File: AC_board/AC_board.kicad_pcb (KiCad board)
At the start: 2 copper layers, 96.5 x 75 mm, 17 parts, among them J1 1226, J2 7471287, J3 Conn_01x02_Male, J4 7471287, J5 7471287, J6 Conn_01x02_Male, K1 G6B-2214P-US-DC12

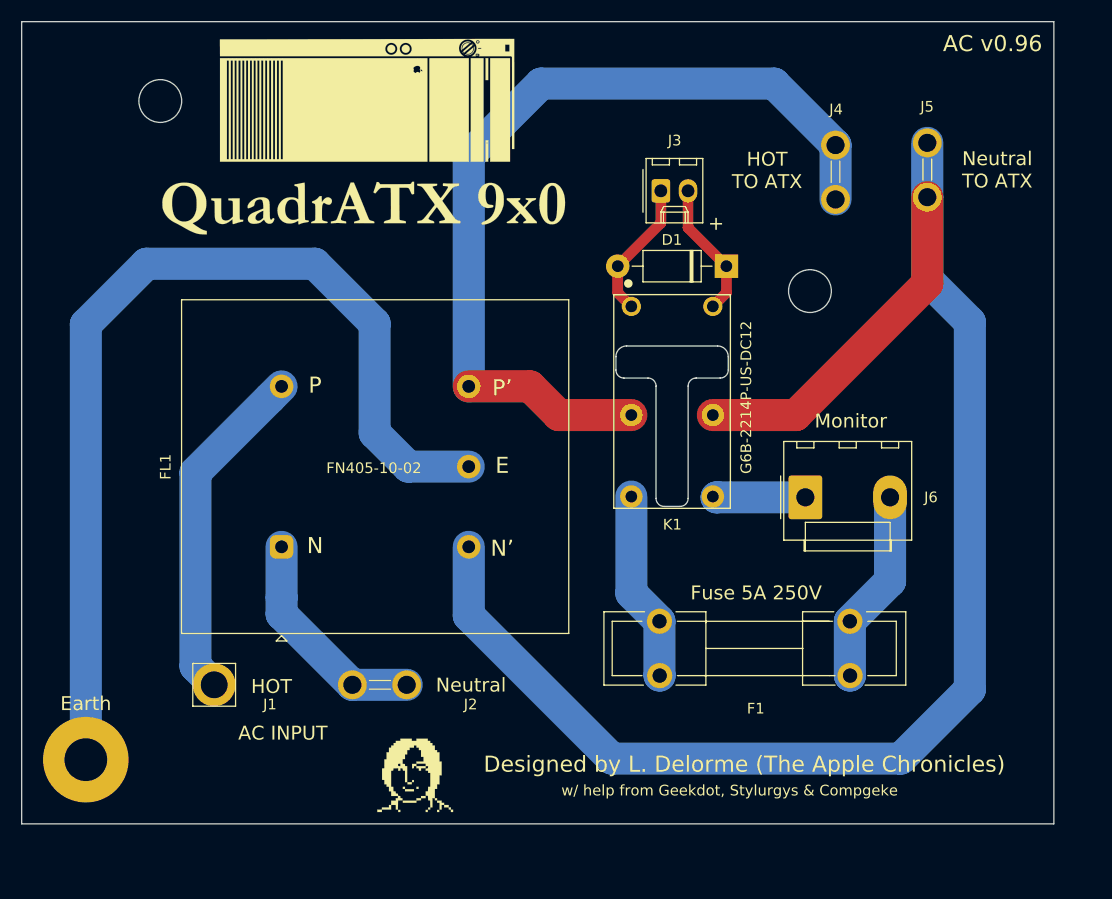
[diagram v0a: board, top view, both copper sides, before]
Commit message: Brand new AC and DC boards
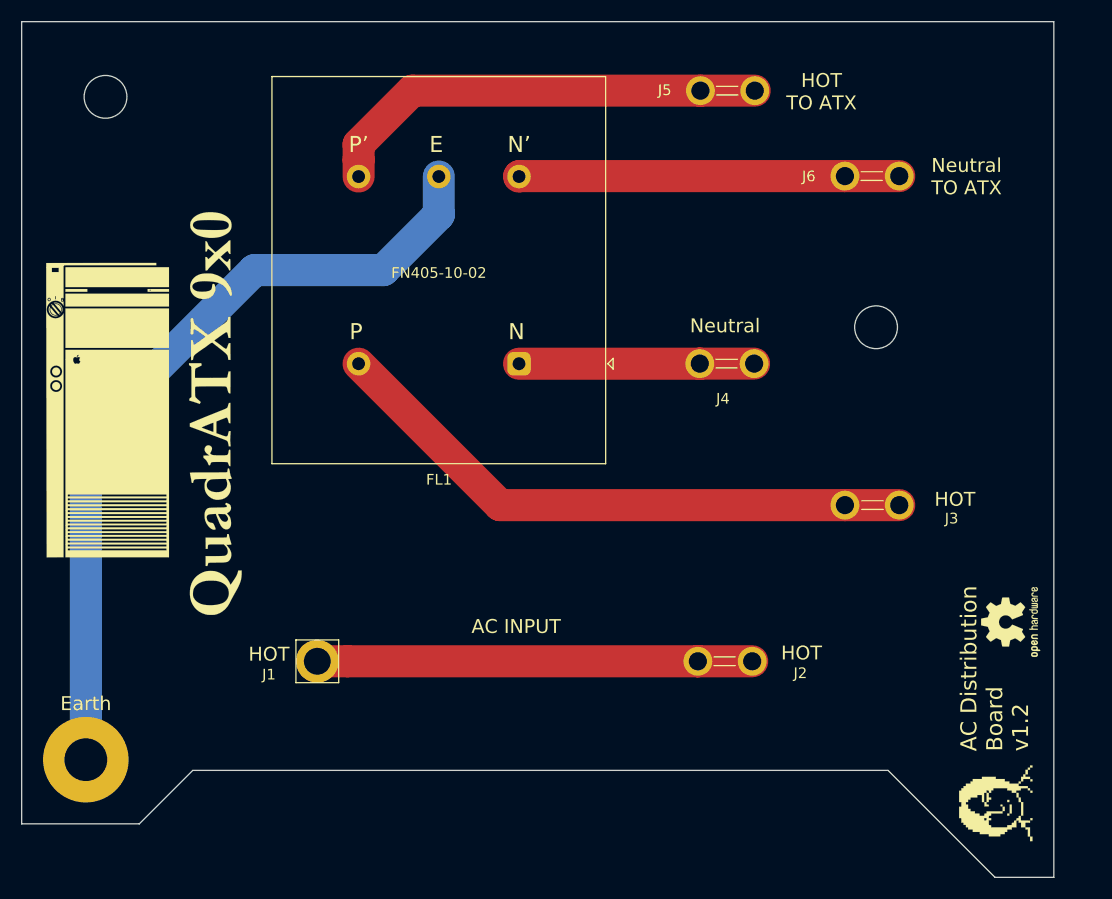
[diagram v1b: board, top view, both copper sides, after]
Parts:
- removed D1: 1N4001, Diode_THT:D_DO-41_SOD81_P10.16mm_Horizontal
- removed F1: Fuse, Fuses_and_Holders_new:Fuseholder5x20_horiz_open_lateral_Type-II
- removed K1: G6B-2214P-US-DC12, Omron_Relay:OM_G6B-2214P-US-DC24
- added REF**: OSHW-Logo2_7.3x6mm_SilkScreen, Symbol:OSHW-Logo2_7.3x6mm_SilkScreen, F.Cu at (161.5, 106.1)
- J3: value Conn_01x02_Male -> 7471287; footprint Connector_Molex:Molex_KK-254_AE-6410-02A_1x02_P2.54mm_Vertical -> Spade_large:7471287_large
- J6: value Conn_01x02_Male -> 7471287; footprint Monitor_Out:Molex_KK-396_2_pin_large -> Spade_large:7471287_large
- moved G*** 55.6 mm to (161.0, 123.4), turned to 90 degrees
- moved G*** 37.8 mm to (77.0, 86.3), turned to 0 degrees
- moved J3 36.9 mm to (151.1, 95.2), turned to 180 degrees
- moved J6 30.3 mm to (146.0, 64.4)
- moved FL1 28.0 mm to (115.5, 82.0), turned to 180 degrees
- moved J2 27.3 mm to (132.2, 109.8), turned to 0 degrees
- moved J4 24.1 mm to (132.4, 82.0), turned to 0 degrees
- moved J5 21.8 mm to (132.5, 56.5), turned to 0 degrees
- moved G*** 21.4 mm to (88.7, 86.6), turned to 90 degrees
- moved J1 9.89 mm to (96.6, 109.8)
- moved REF** 7.04 mm to (148.9, 78.6)
- moved REF** 5.13 mm to (76.8, 57.0)
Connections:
- FL1 pad 1: Net-(FL1-Pad1) -> /Neutral_SW
- FL1 pad 2: Net-(FL1-Pad2) -> /Neutral_Out
- FL1 pad 4: Net-(FL1-Pad4) -> /Phase_Out
- FL1 pad 5: Net-(FL1-Pad5) -> /Phase_SW
- J1 pad 1: Net-(FL1-Pad5) -> /Phase_Input
- J2 pad 1: Net-(FL1-Pad1) -> /Phase_Input
- J2 pad 2: Net-(FL1-Pad1) -> /Phase_Input
- J3 pad 1: Net-(D1-Pad2) -> /Phase_SW
- J3 pad 2: Net-(D1-Pad1) -> /Phase_SW
- J4 pad 1: Net-(FL1-Pad4) -> /Neutral_SW
- J4 pad 2: Net-(FL1-Pad4) -> /Neutral_SW
- J5 pad 1: Net-(FL1-Pad2) -> /Phase_Out
- J5 pad 2: Net-(FL1-Pad2) -> /Phase_Out
- J6 pad 1: Net-(J6-Pad1) -> /Neutral_Out
- J6 pad 2: Net-(F1-Pad2) -> /Neutral_Out
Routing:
- net Net-(FL1-Pad2): track 147.5 -> 0.00 mm
- net Net-(FL1-Pad4): track 82.5 -> 0.00 mm
- net /Phase_SW: track 0.00 -> 56.0 mm
- net /Phase_Out: track 0.00 -> 42.1 mm
- net /Phase_Input: track 0.00 -> 40.7 mm
- net /Neutral_Out: track 0.00 -> 35.6 mm
- net Net-(FL1-Pad5): track 32.0 -> 0.00 mm
- net /Neutral_SW: track 0.00 -> 22.0 mm
- net Net-(FL1-Pad1): track 20.7 -> 0.00 mm
- net Net-(F1-Pad2): track 18.2 -> 0.00 mm
- net Net-(F1-Pad1): track 17.8 -> 0.00 mm
- net Earth: track 92.7 -> 75.2 mm
- net Net-(D1-Pad2): track 13.0 -> 0.00 mm
- net Net-(D1-Pad1): track 12.8 -> 0.00 mm
- net Net-(J6-Pad1): track 8.34 -> 0.00 mm
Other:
- board size 96.5 x 75 mm -> 96.5 x 80 mm
- net class Earth: clearance 4 -> 2.5
- net class Power AC: clearance 5 -> 4.5
- board text added: "AC Distribution Board v1.2"
- board text removed: "+"
- board text removed: "AC v0.96"
- board text removed: "Designed by L. Delorme (The Apple Chronicles)"
- board text removed: "Fuse 5A 250V"
- board text removed: "G6B-2214P-US-DC12"
- board text removed: "Monitor"
- board text removed: "w/ help from Geekdot, Stylurgys & Compgeke"
